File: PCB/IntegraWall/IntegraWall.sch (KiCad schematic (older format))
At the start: 5 parts, among them J1 Raspberry_Pi_2_3

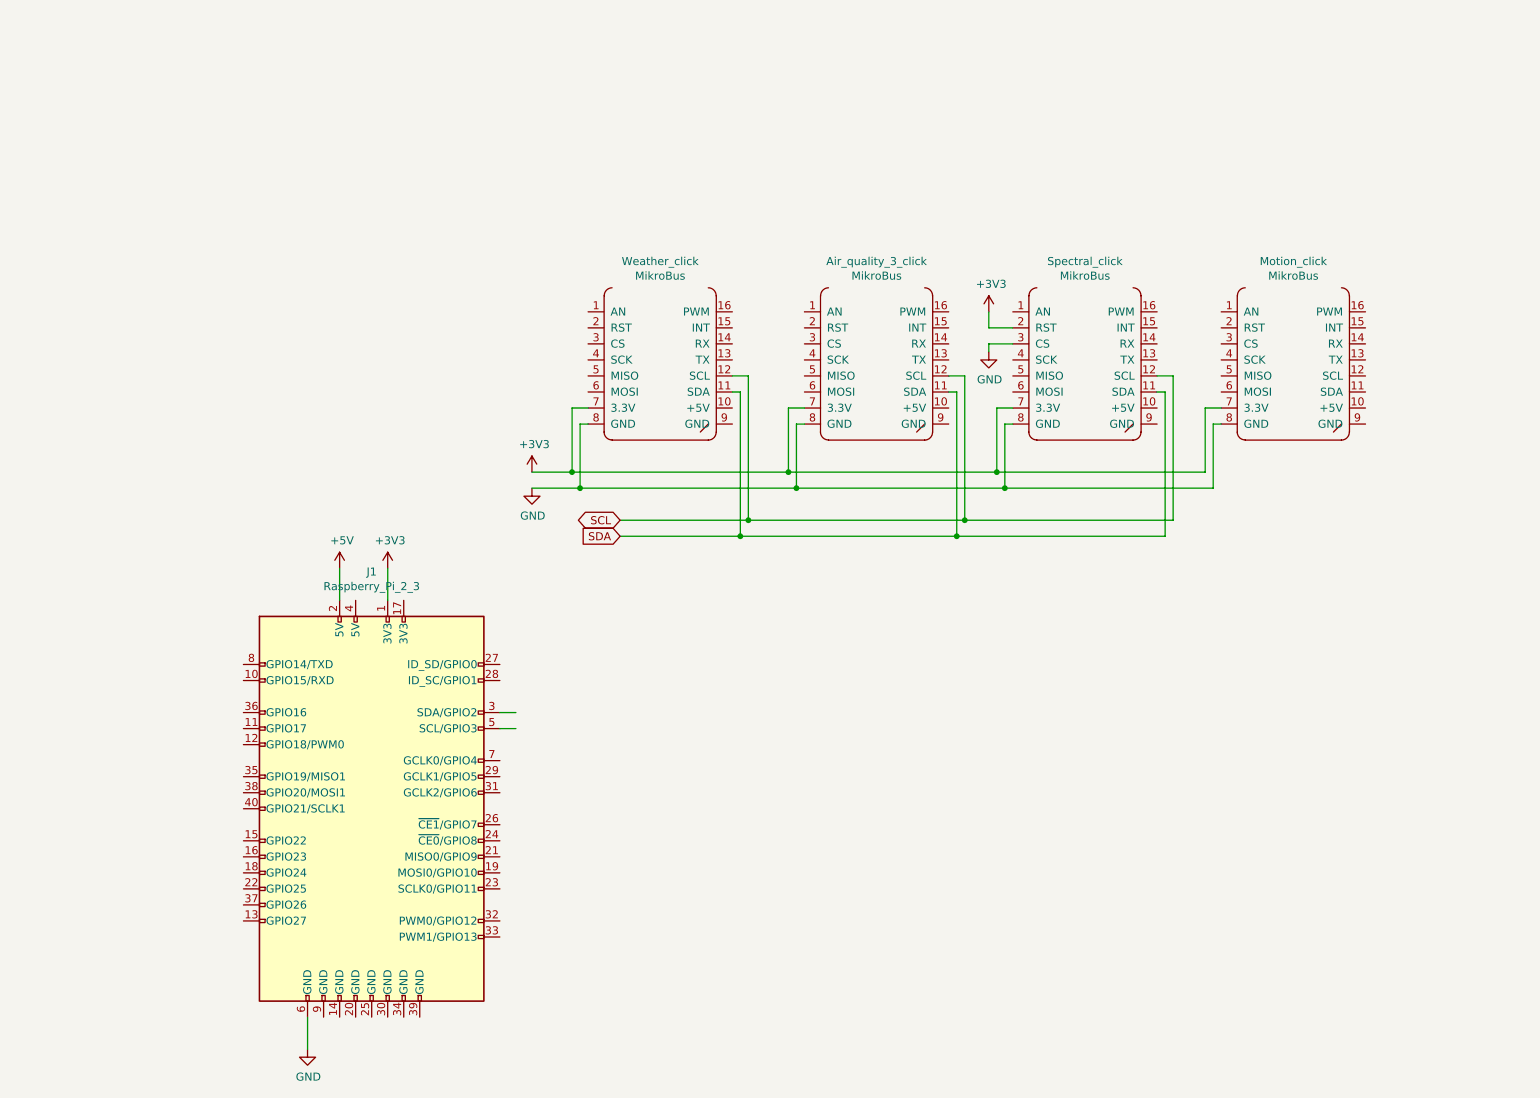
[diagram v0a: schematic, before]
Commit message: Added the dust sensor and finnished the PCB
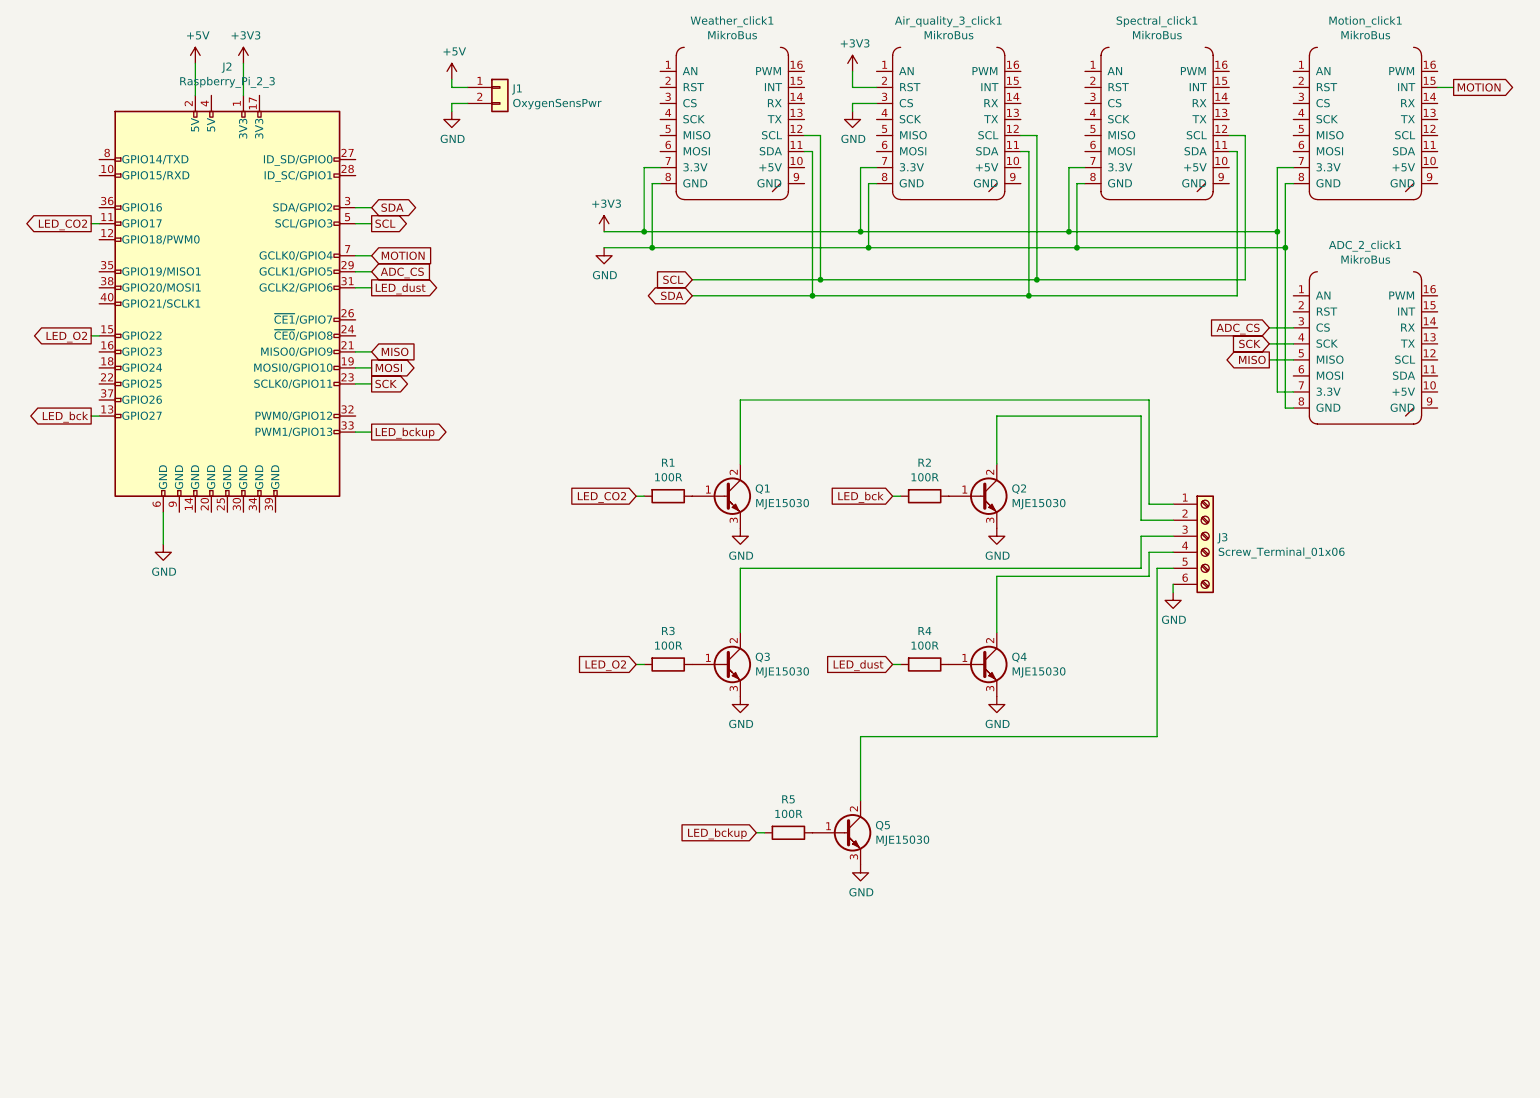
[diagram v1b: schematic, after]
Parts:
- added ADC_2_click1: MikroBus, Click_boards:Click_board, symbol ClickBoards:MikroBus
- added J1: OxygenSensPwr, Connector_PinHeader_2.54mm:PinHeader_1x02_P2.54mm_Horizontal, symbol Connector_Generic:Conn_01x02
- added J3: Screw_Terminal_01x06, TerminalBlock:TerminalBlock_bornier-6_P5.08mm, symbol Connector:Screw_Terminal_01x06
- added Q1, Q2, Q3, Q4, Q5: MJE15030, Package_TO_SOT_THT:TO-220-3_Vertical, symbol Transistor_BJT:MJE13009G
- added R1, R2, R3, R4, R5: 100R, Resistor_SMD:R_1206_3216Metric_Pad1.42x1.75mm_HandSolder, symbol Device:R
- Air_quality_3_click1: renamed from Air_quality_3_click; footprint (none) -> Click_boards:Air_quality_click
- Motion_click1: renamed from Motion_click; footprint (none) -> Click_boards:Click_board
- Spectral_click1: renamed from Spectral_click; footprint (none) -> Click_boards:Spectral_click
- Weather_click1: renamed from Weather_click; footprint (none) -> Click_boards:Click_board
- renumbered J1 to J2
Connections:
- net labels added: ADC_CS, LED_CO2, LED_O2, LED_bck, LED_bckup, LED_dust, MISO, MOSI, MOTION, SCK
- wire segments 51 -> 99
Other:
- moved on the sheet: Air_quality_3_click1, J2, Motion_click1, Spectral_click1, Weather_click1
